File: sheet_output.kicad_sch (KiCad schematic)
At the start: 9 parts, among them J2 TRRS PJ-3X4S (CTIA, bottom-si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

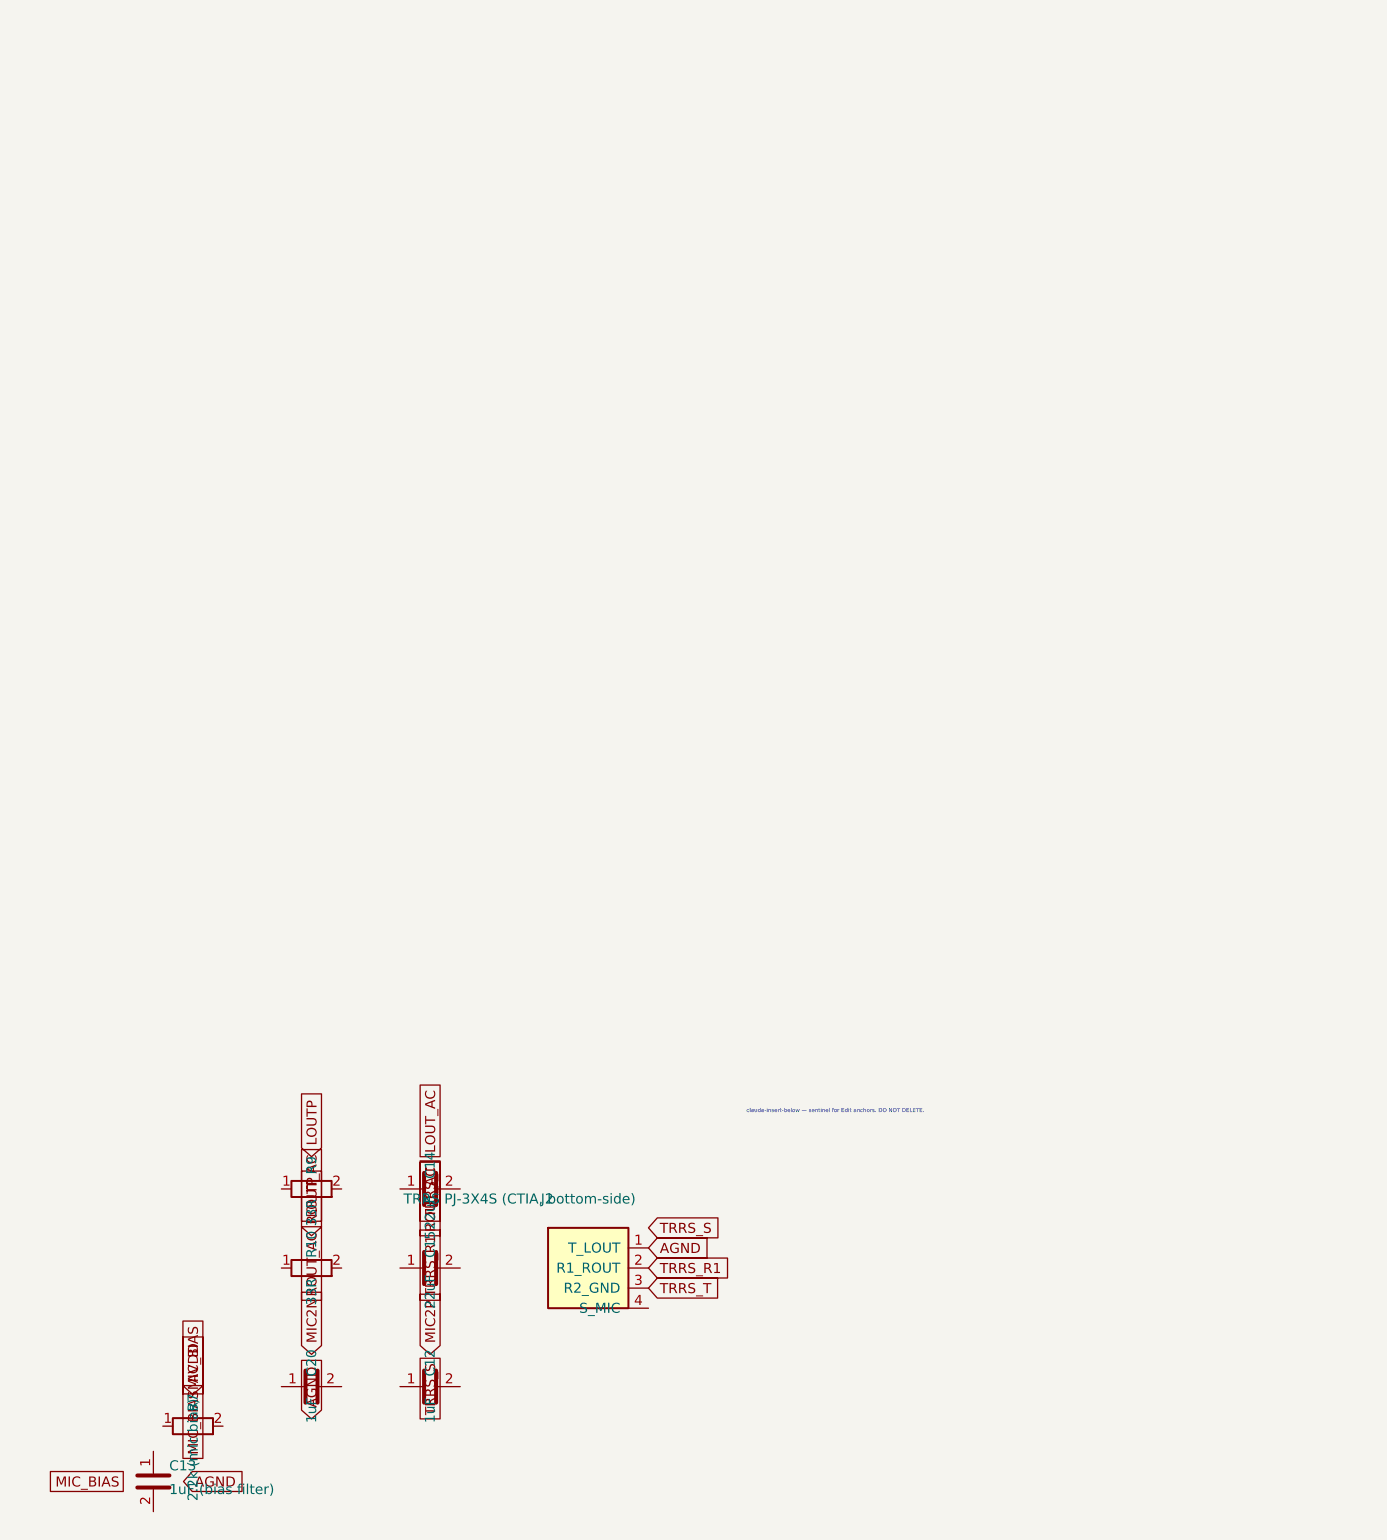
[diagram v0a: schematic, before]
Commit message: design: full iteration since init — codec, phantom/PoE, LDO, BOM, fab
First substantive commit since init; captures the entire design
iteration and quiets KiCad churn in-repo.

Codec / PCB
- ES8389: custom QFN-24 0.35mm land pattern (ES8389_QFN24_P0.35mm)
- Corrected mirror-reversed codec I2C/I2S pins
- Un-mirrored all B.Cu footprints that imported un-flipped
  (U1, OK1, Q1, D2, D6-D8 + silk)
- Re-coupled schematic to PCB netlist -> IN SYNC

Phantom / PoE
- F1 -> 1812L010/60DR (100mA hold / 60V, true 1812)
- Q1 -> Si2325DS (150V) for PoE++ margin
- Added SW1 SS-12D00-G3 slide switch = manual phantom enable (frees GPIO15)
- D8/R15/R16 phantom-present LED rework
- Confirmed PoE tap: BD1/BD2 (MB10F) -> VDD/VSS -> J5 pin 1/2

Power / connectors
- Added low-noise analog LDO U2 TPS7A2033 (+C21/C22): +5V -> +3V3_A -> AVDD
- J1 -> Neutrik NCJ6FA-H switched combo (+ 3D model)

Project
- BOM: single source of truth BOM.csv (JLCPCB-uploadable); removed BOM.md
- Added fab/ outputs (gerbers, drill, CPL) and tools/ (check_sync.py, relabel_sch.py)
- .gitignore: ignore KiCad churn (*.kicad_prl, *-drc.rpt, *-erc.rpt, backups) + local docs
- Untrack scramble_hat-erc.rpt (now ignored)
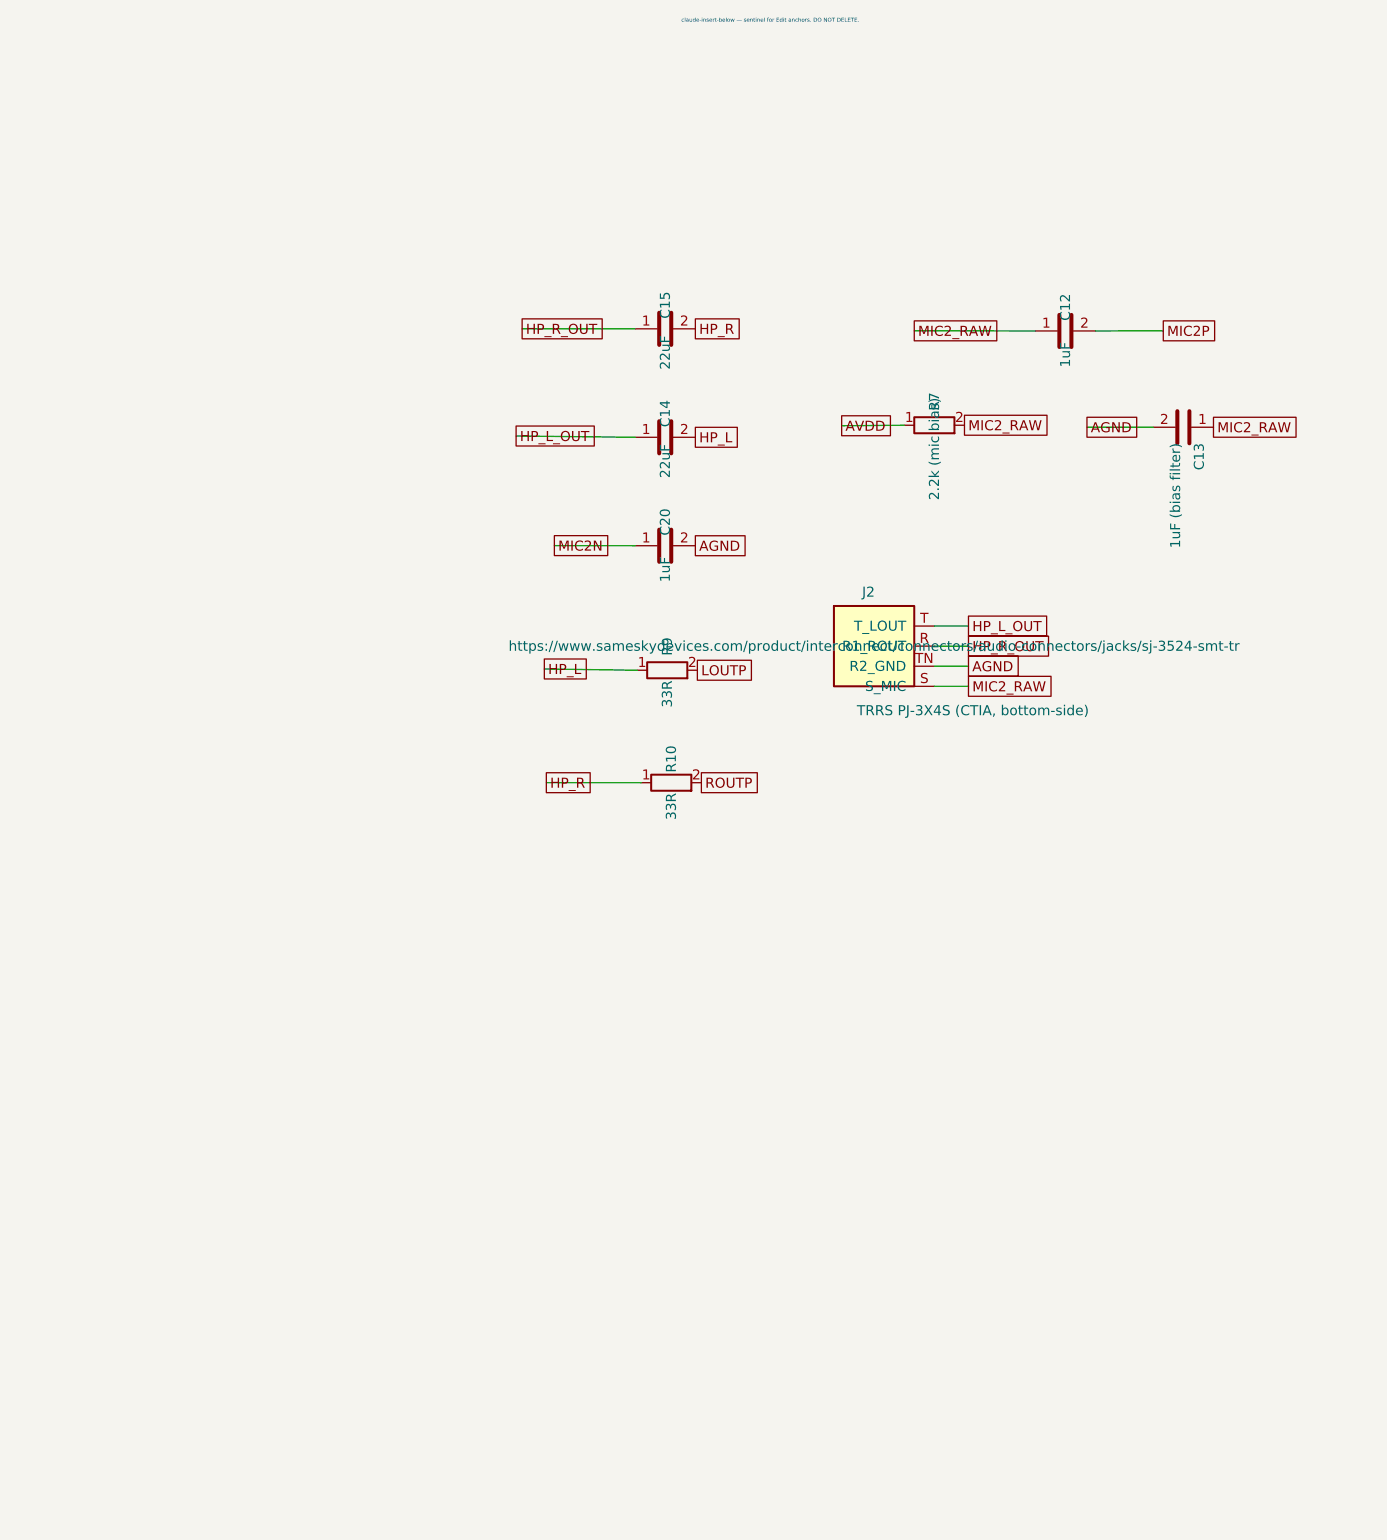
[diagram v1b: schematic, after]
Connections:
- net AGND: now also C13.2, C20.2, J2.TN (R2_GND); no longer J2.1 (T_LOUT)
- net AVDD: now also R7.1
- net LOUTP: now also R9.2
- net MIC2N: now also C20.1
- net MIC2P: now also C12.2
- net ROUTP: now also R10.2
- net HP_L: now reaches R9.1
- net HP_L: now also C14.2
- net HP_R: now reaches R10.1
- net HP_R: now also C15.2
- net HP_L_OUT: now reaches C14.1
- net HP_L_OUT: now also J2.T (T_LOUT)
- net HP_R_OUT: now reaches C15.1
- net HP_R_OUT: now also J2.R (R1_ROUT)
- net MIC2_RAW: now reaches C12.1
- net MIC2_RAW: now also C13.1, J2.S (S_MIC), R7.2
- removed net TRRS_R1: J2.2 (R1_ROUT)
- removed net TRRS_T: J2.3 (R2_GND)
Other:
- moved on the sheet: C12, C13, C14, C15, C20, J2, R10, R7, R9
